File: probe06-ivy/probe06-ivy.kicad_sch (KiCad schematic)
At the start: 31 parts, among them SW1 SW_Push, U1 STM32F407VGTx, Y1 8 MHz, Y2 32.768 KHz

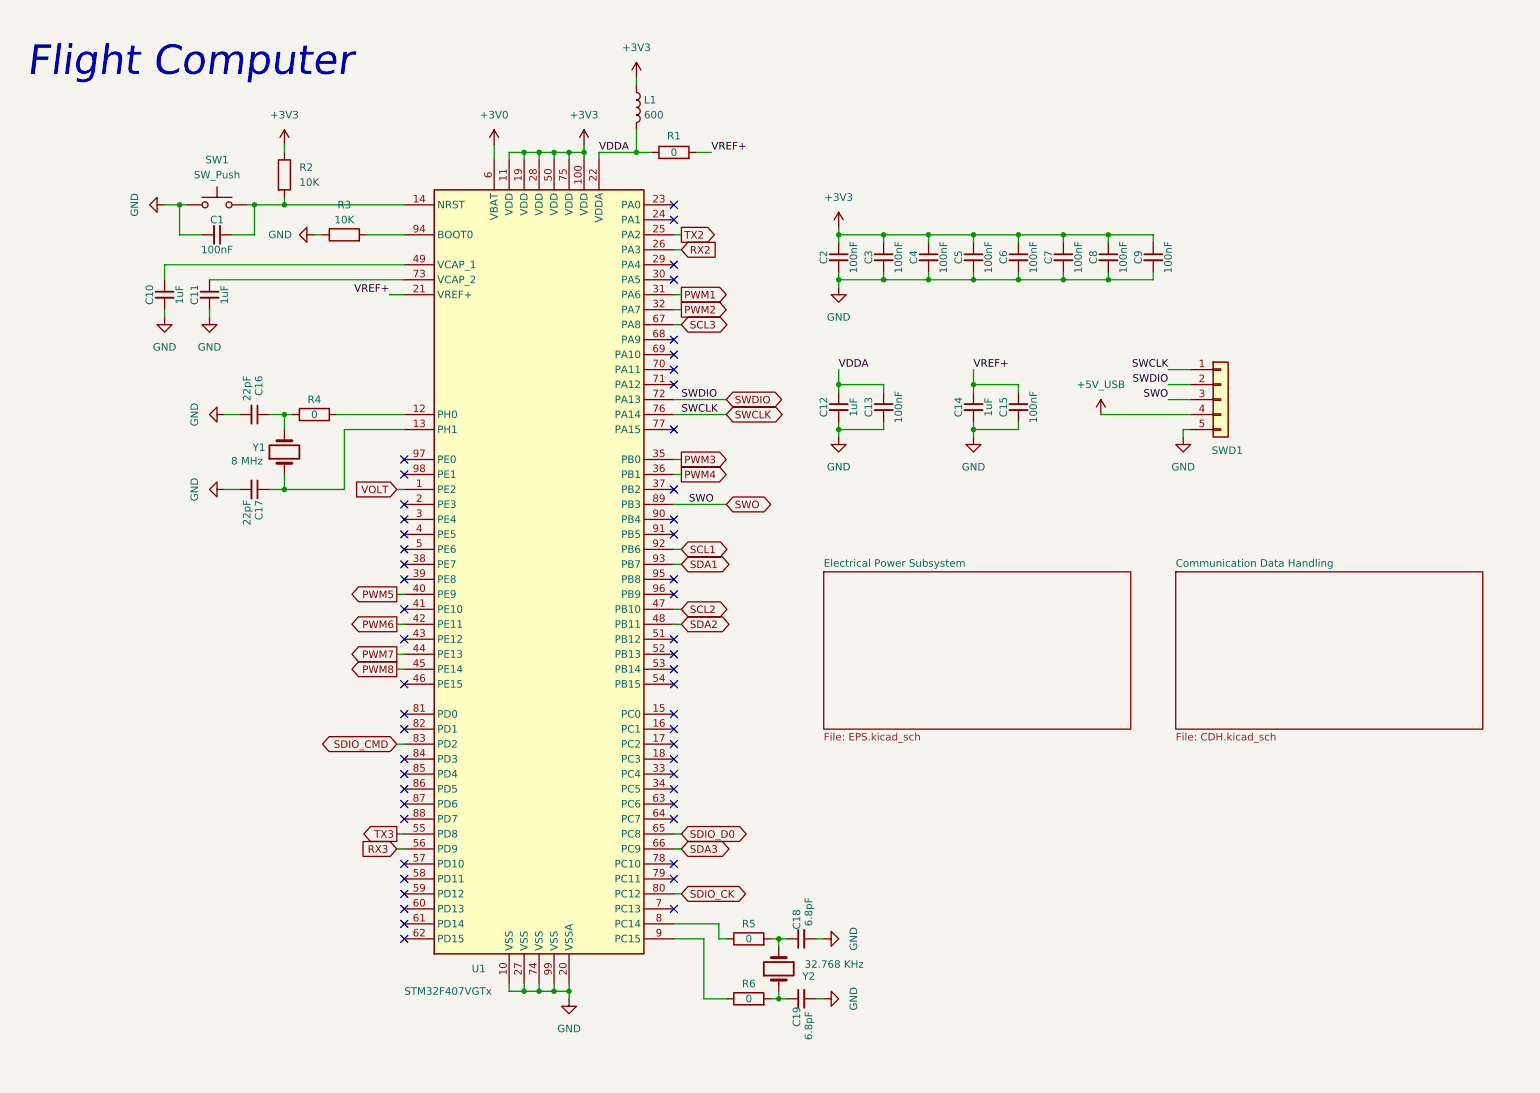
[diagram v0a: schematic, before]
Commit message: Routing Layout - add footprint to all components - pcb shape and dimension - component placement
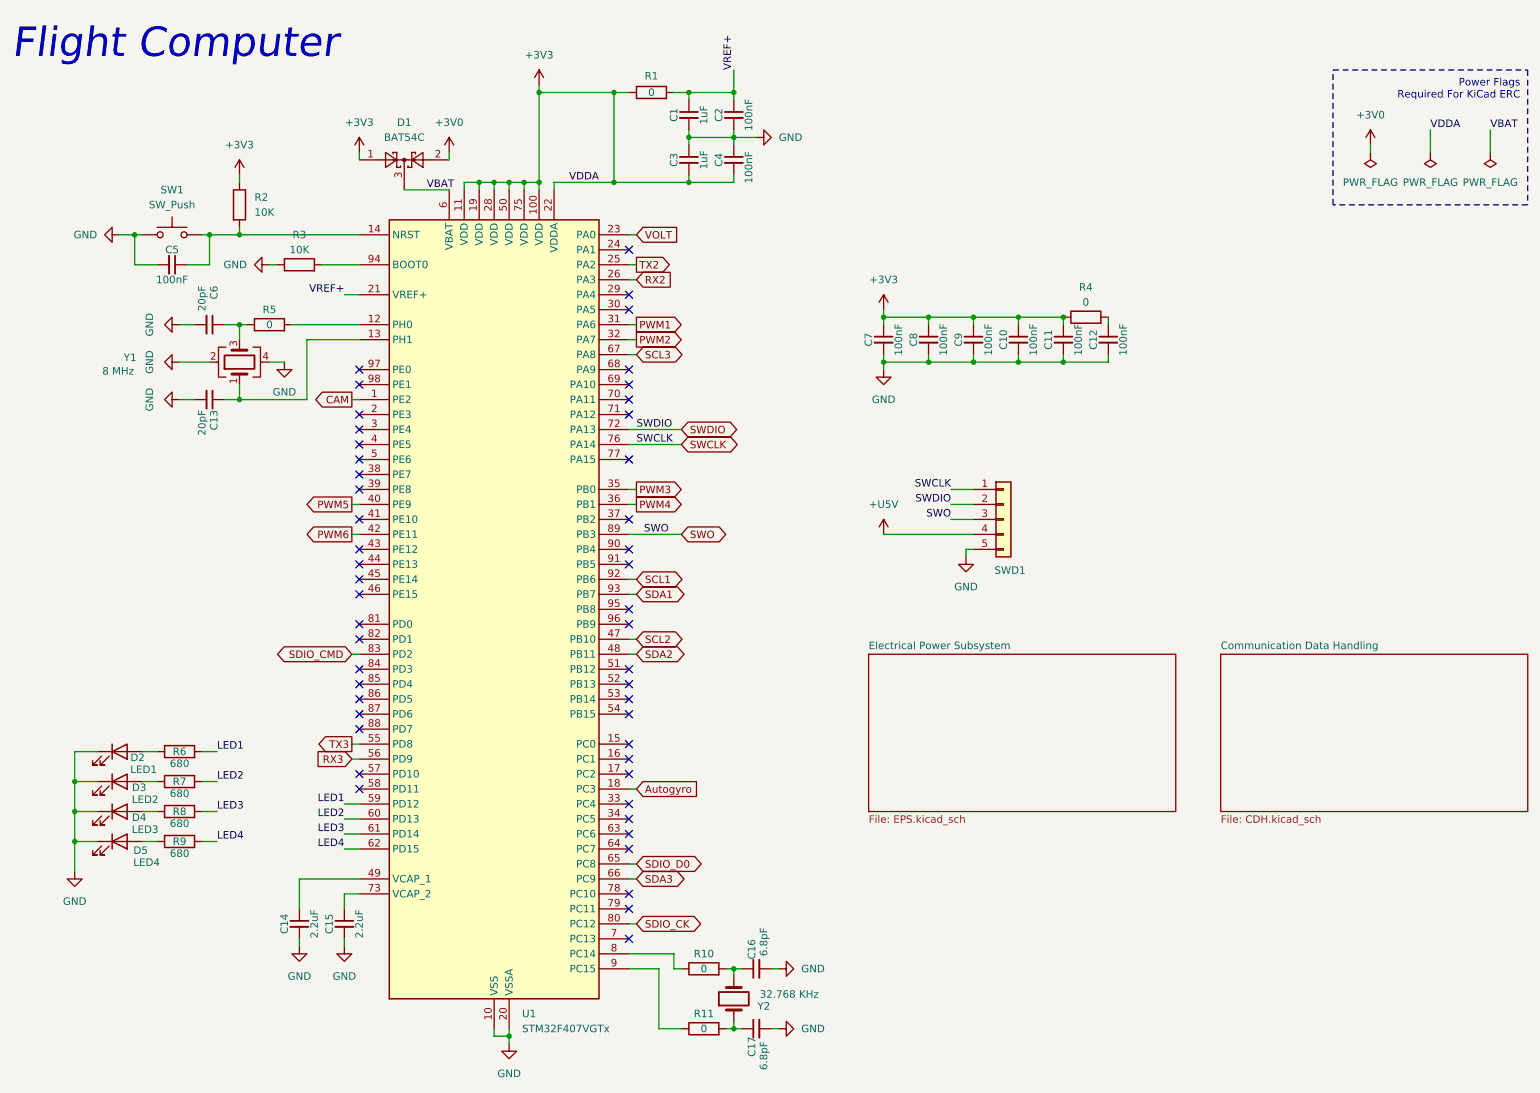
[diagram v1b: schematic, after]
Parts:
- removed C10, C11, C12: 1uF, Capacitor_SMD:C_0805_2012Metric, symbol Device:C_Small
- removed C18, C19: 6.8pF, Capacitor_SMD:C_0805_2012Metric, symbol Device:C_Small
- removed C8, C9: 100nF, Capacitor_SMD:C_0805_2012Metric, symbol Device:C_Small
- removed L1: 600, symbol Device:L
- removed Y1: 8 MHz, Crystal:Crystal_HC49-U_Vertical, symbol Device:Crystal
- added C2, C4, C5: 100nF, Capacitor_SMD:C_0805_2012Metric, symbol Device:C_Small
- added C3: 1uF, Capacitor_SMD:C_0805_2012Metric, symbol Device:C_Small
- added C6: 20pF, Capacitor_SMD:C_0805_2012Metric, symbol Device:C_Small
- added D1: BAT54C, Package_TO_SOT_SMD:SOT-23, symbol Diode:BAT54C
- added D2: LED1, LED_SMD:LED_0805_2012Metric, symbol Device:LED
- added D3: LED2, LED_SMD:LED_0805_2012Metric, symbol Device:LED
- added D4: LED3, LED_SMD:LED_0805_2012Metric, symbol Device:LED
- added D5: LED4, LED_SMD:LED_0805_2012Metric, symbol Device:LED
- added R10, R11: 0, Resistor_SMD:R_0805_2012Metric, symbol Device:R
- added R7, R8, R9: 680, Resistor_SMD:R_0805_2012Metric, symbol Device:R
- added Y1: 8 MHz, Crystal:Crystal_SMD_3225-4Pin_3.2x2.5mm, symbol Device:Crystal_GND24
- C1: value 100nF -> 1uF
- C13: value 100nF -> 20pF
- C14: value 1uF -> 2.2uF
- C15: value 100nF -> 2.2uF
- C16, C17: value 22pF -> 6.8pF
- R1, R3, R4, R5: footprint (none) -> Resistor_SMD:R_0805_2012Metric
- R6: value 0 -> 680; footprint (none) -> Resistor_SMD:R_0805_2012Metric
- SW1: footprint (none) -> Button_Switch_SMD:SW_SPST_FSMSM
- SWD1: footprint (none) -> Connector_JST:JST_XH_B5B-XH-A_1x05_P2.50mm_Vertical
- renumbered C5 to C10, C6 to C11, C7 to C12, C2 to C7, C3 to C8, C4 to C9
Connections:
- net +3V0: now also D1.2; no longer U1.6 (VBAT)
- net +3V3: now also R1.1, R4.1, U1.22 (VDDA), C3.2, C4.2, D1.1; no longer C12.1
- net GND: now also C2.2, C3.1, C4.1, C5.2, C6.2, D2.1 (K), D3.1 (K), D4.1 (K), D5.1 (K), Y1.2, Y1.4
- net VOLT: now also U1.23 (PA0); no longer U1.1 (PE2)
- net VREF+: now also C1.1, C2.1; no longer C14.1, C15.1
- net at U1.13 (PH1): now also C13.1, Y1.1; no longer C17.1
- net at C16.1: now also Y2.2, R10.2; no longer R4.1
- net at R4.2: now also C12.1; no longer U1.12 (PH0)
- net at R5.1: now also C6.1, Y1.3; no longer U1.8 (PC14)
- net at R5.2: now also U1.12 (PH0); no longer Y2.2
- net at U1.73 (VCAP_2): now also C15.1
- net at R2.2, SW1.2, U1.14 (NRST): now also C5.1; no longer C1.1
- net Autogyro: now reaches U1.18 (PC3)
- net at U1.49 (VCAP_1): now also C14.1
- net LED1: now reaches U1.59 (PD12)
- net LED1: now also R6.2
- net LED2: now reaches U1.60 (PD13)
- net LED2: now also R7.2
- net LED3: now reaches U1.61 (PD14)
- net LED3: now also R8.2
- net LED4: now reaches U1.62 (PD15)
- net LED4: now also R9.2
- net at R6.1: now also D2.2 (A); no longer U1.9 (PC15)
- net at Y2.1: now also C17.1, R11.2; no longer R6.2
- net +5V_USB renamed +U5V
- net PWM7: no longer names the net of U1.44 (PE13)
- net PWM8: no longer names the net of U1.45 (PE14)
- removed net VDDA: C13.1, R1.1, U1.22 (VDDA)
- new net: D5.2 (A), R9.1
- new net: R10.1, U1.8 (PC14)
- new net: R11.1, U1.9 (PC15)
- new net: D4.2 (A), R8.1
- new net: D3.2 (A), R7.1
- new net CAM: U1.1 (PE2)
- new net VBAT: D1.3, U1.6 (VBAT)
- no-connect marks 53 -> 49
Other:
- note added: "Power Flags Required For KiCad ERC"
- title: CanSat Avionics -> CanSat Avionics - Auto Gyro Descender
- moved on the sheet: C10, C11, C12, C7, C8, C9, SWD1

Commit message: Routing (2) - make the pcb edge cuts to suit mechanic requirements - route some components (power, usb debug, gps) progress 50%
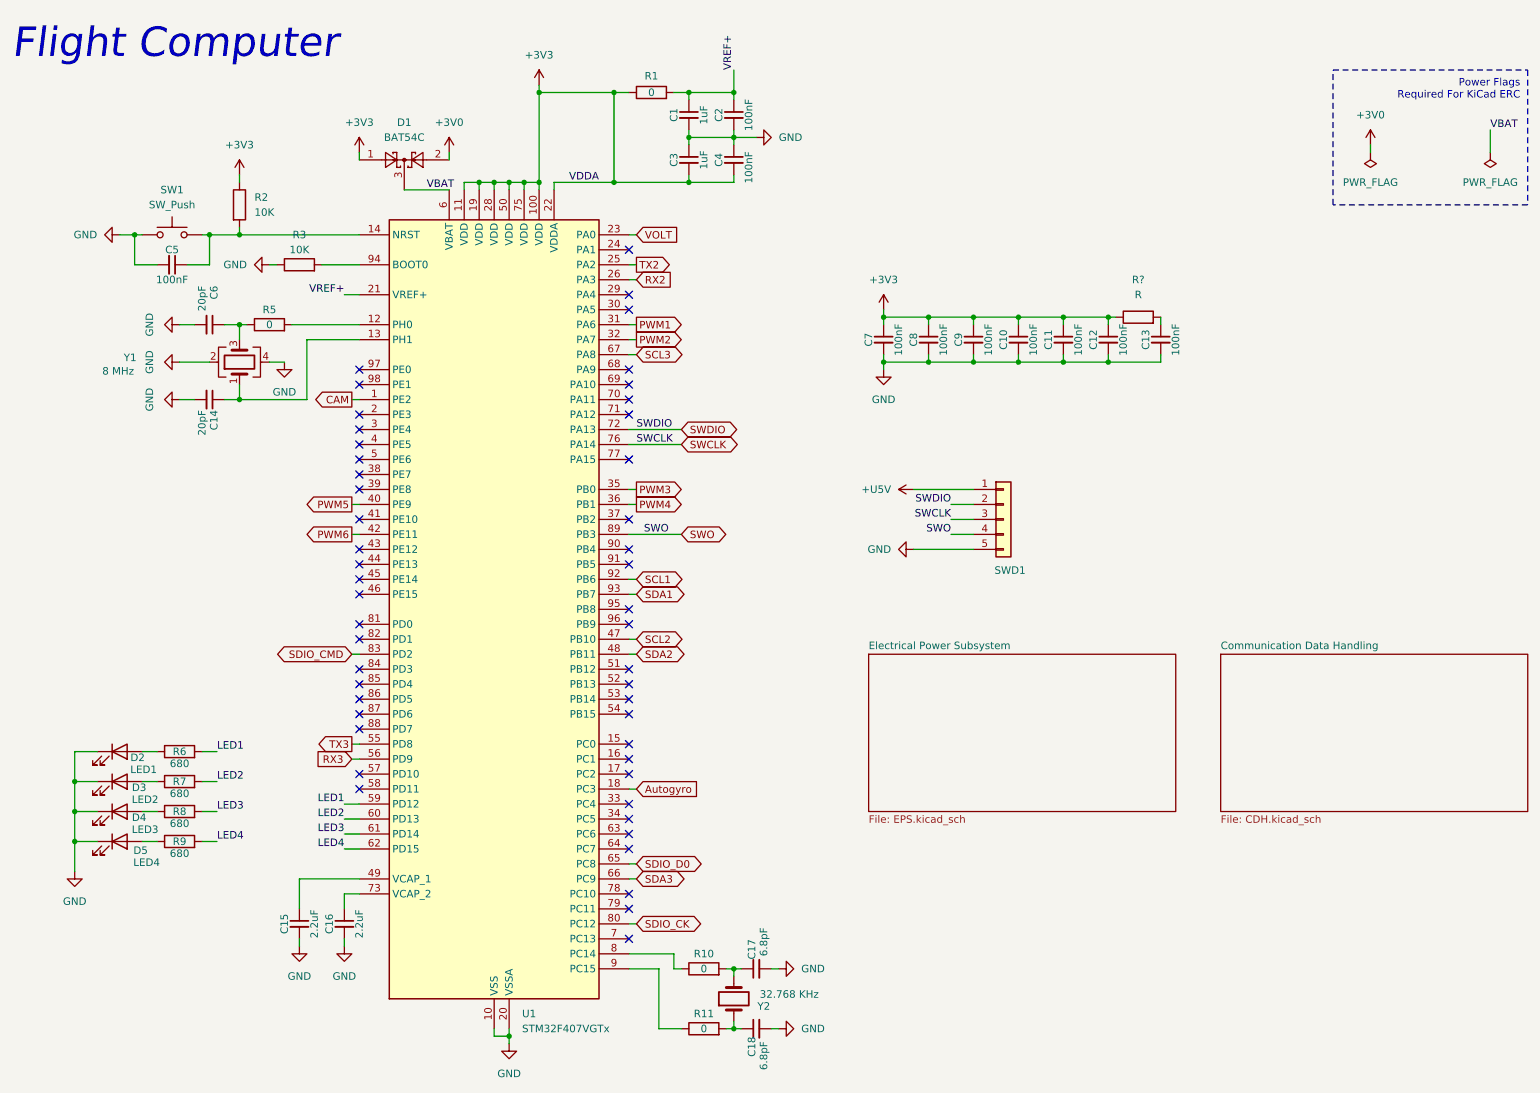
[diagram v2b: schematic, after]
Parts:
- removed R4: 0, Resistor_SMD:R_0805_2012Metric, symbol Device:R
- added C13: 100nF, Capacitor_SMD:C_0603_1608Metric, symbol Device:C_Small
- added R?: R, symbol Device:R
- C1, C10, C11, C12, C2, C3, C4, C5, C6, C7, C8, C9: footprint Capacitor_SMD:C_0805_2012Metric -> Capacitor_SMD:C_0603_1608Metric
- C14: renamed from C13; footprint Capacitor_SMD:C_0805_2012Metric -> Capacitor_SMD:C_0603_1608Metric
- C15: renamed from C14; footprint Capacitor_SMD:C_0805_2012Metric -> Capacitor_SMD:C_0603_1608Metric
- C16: renamed from C15; footprint Capacitor_SMD:C_0805_2012Metric -> Capacitor_SMD:C_0603_1608Metric
- C17: renamed from C16; footprint Capacitor_SMD:C_0805_2012Metric -> Capacitor_SMD:C_0603_1608Metric
- C18: renamed from C17; footprint Capacitor_SMD:C_0805_2012Metric -> Capacitor_SMD:C_0603_1608Metric
- D2, D3, D4, D5: footprint LED_SMD:LED_0805_2012Metric -> LED_SMD:LED_0603_1608Metric
- R1, R10, R11, R2, R3, R5, R6, R7, R8, R9: footprint Resistor_SMD:R_0805_2012Metric -> Resistor_SMD:R_0603_1608Metric
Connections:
- net +3V3: now also C12.1, R?.1
- net +U5V: now also SWD1.1 (Pin_1); no longer SWD1.4 (Pin_4)
- net GND: now also C13.2
- net SWCLK: now also SWD1.3 (Pin_3); no longer SWD1.1 (Pin_1)
- net SWO: now also SWD1.4 (Pin_4); no longer SWD1.3 (Pin_3)
- new net: C13.1, R?.2
